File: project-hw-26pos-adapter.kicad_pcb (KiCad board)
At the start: 4 copper layers, 38 x 52 mm, 23 parts, among them J1 SM04B-SRSS-TB(LF)(SN), J2 3220-26-0300-00, U1 Pink Panda v2.1.0

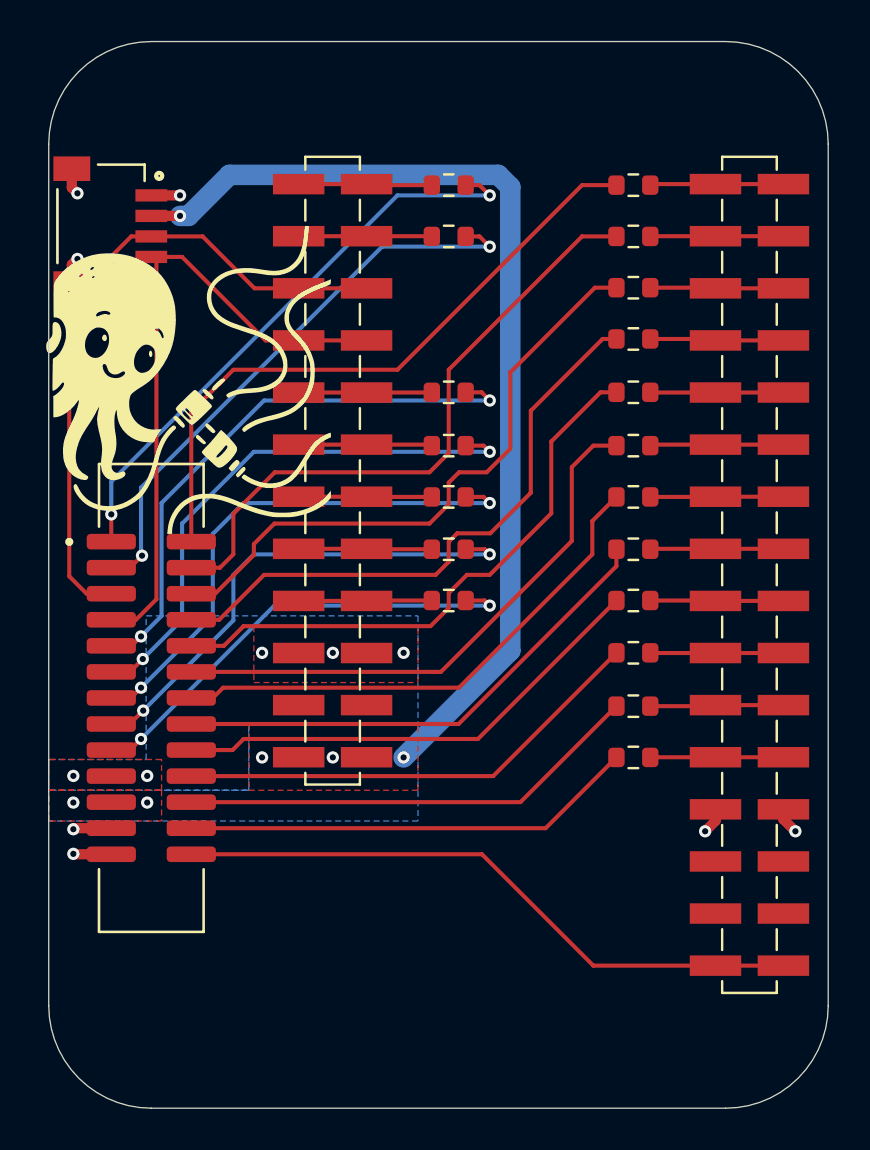
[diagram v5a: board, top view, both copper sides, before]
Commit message: Also add series resistors to SDA/SCL
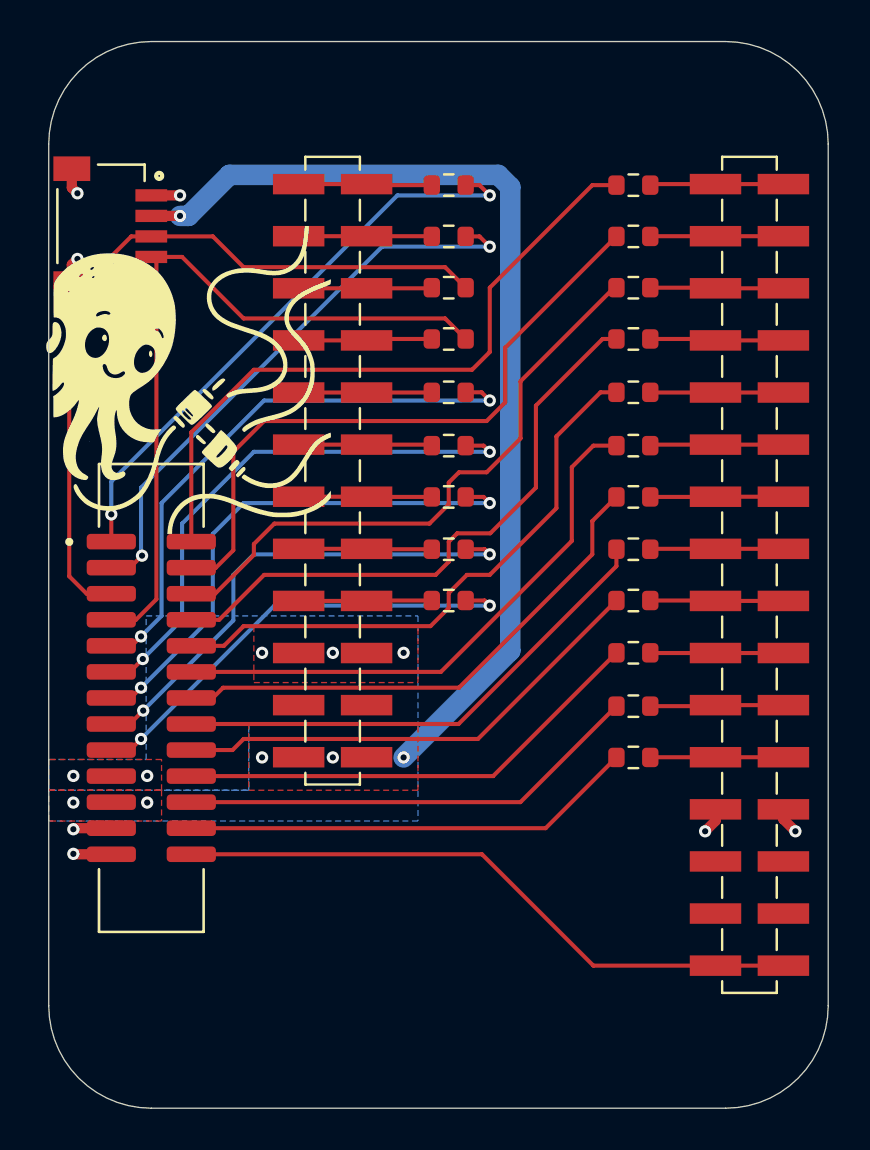
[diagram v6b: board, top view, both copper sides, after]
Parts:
- added R20: R_Small, Resistor_SMD:R_0603_1608Metric, F.Cu at (51.5, 31.0)
- added R21: R_Small, Resistor_SMD:R_0603_1608Metric, F.Cu at (51.5, 33.5)
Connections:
- U1 pad 3: /P0.04 -> Net-(U1-P0.04)
- U1 pad 4: /P0.26 -> Net-(U1-P0.26)
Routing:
- net Net-(U1-P0.26): track 0.00 -> 6.52 mm
- net Net-(U1-P0.04): track 0.00 -> 6.50 mm
- net /P0.04: track 32.7 -> 37.6 mm
- net /P0.26: track 31.6 -> 36.4 mm
- net /P0.20: track 31.6 -> 32.9 mm
- net /P0.21: track 31.0 -> 32.0 mm
- net /P0.15: track 30.0 -> 29.5 mm

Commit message: pcb: add a few ground vias
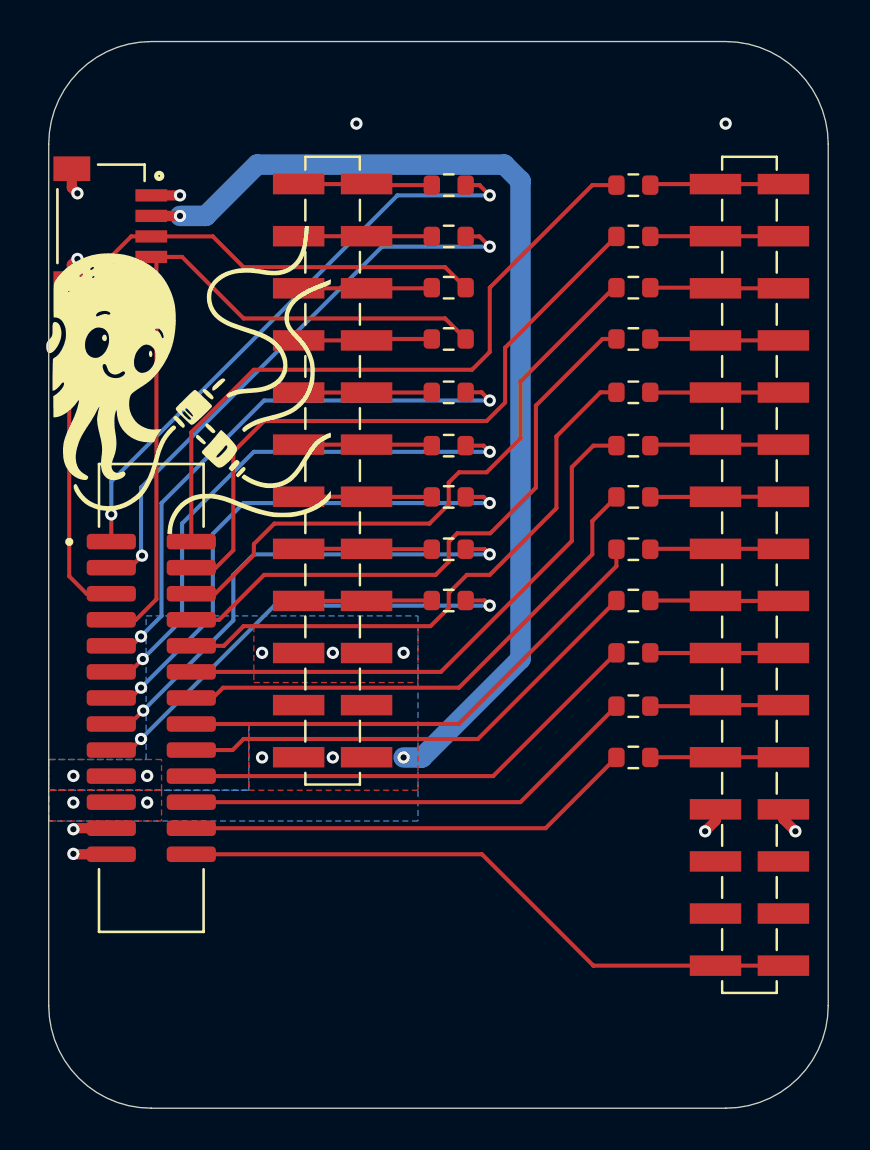
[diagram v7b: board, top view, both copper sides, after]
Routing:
- net /VDD_OUT: track 48.5 -> 50.4 mm
- net GND: vias 7 -> 9
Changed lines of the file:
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@@
+	)
+	(via
+		(at 47 23)
+		(size 0.6)
+		(drill 0.3)
+		(layers "F.Cu" "B.Cu")
+		(free yes)
+		(net 1)
 	)
 	(via
@@
 		(drill 0.3)
 		(layers "F.Cu" "B.Cu")
+		(net 1)
+	)
+	(via
+		(at 65 23)
+		(size 0.6)
+		(drill 0.3)
+		(layers "F.Cu" "B.Cu")
+		(free yes)
 		(net 1)
 	)
@@
 	)
 	(segment
-		(start 54.5 26.085786)
-		(end 53.914214 25.5)
+		(start 39.657107 27.5)
+		(end 38.4 27.5)
+		(width 1)
+		(layer "B.Cu")
+		(net 3)
+	)
+	(segment
+		(start 42.157107 25)
+		(end 39.657107 27.5)
+		(width 1)
+		(layer "B.Cu")
+		(net 3)
+	)
+	(segment
+		(start 55 25.792893)
+		(end 54.207107 25)
+		(width 1)
+		(layer "B.Cu")
+		(net 3)
+	)
+	(segment
+		(start 50.2 53.9)
+		(end 55 49.1)
+		(width 1)
+		(layer "B.Cu")
+		(net 3)
+	)
+	(segment
+		(start 55 49.1)
+		(end 55 25.792893)
 		(width 1)
 		(layer "B.Cu")
@@
 	(segment
 		(start 49.3 53.9)
-		(end 54.5 48.7)
-		(width 1)
-		(layer "B.Cu")
-		(net 3)
-	)
-	(segment
-		(start 54.5 48.7)
-		(end 54.5 26.085786)
-		(width 1)
-		(layer "B.Cu")
-		(net 3)
-	)
-	(segment
-		(start 53.914214 25.5)
-		(end 40.814214 25.5)
-		(width 1)
-		(layer "B.Cu")
-		(net 3)
-	)
-	(segment
-		(start 40.814214 25.5)
-		(end 38.814214 27.5)
-		(width 1)
-		(layer "B.Cu")
-		(net 3)
-	)
-	(segment
-		(start 38.814214 27.5)
-		(end 38.4 27.5)
-		(width 1)
-		(layer "B.Cu")
+		(end 50.2 53.9)
+		(width 1)
+		(layer "B.Cu")
+		(net 3)
+	)
+	(segment
+		(start 54.207107 25)
+		(end 42.157107 25)
+		(width 1)
+		(layer "B.Cu")

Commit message: pcb: update version on silkscreen
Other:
- board text added: "v1.0.0-5-gc464fd8"
- board text removed: "v1.0.0-2-g7777ac5"
